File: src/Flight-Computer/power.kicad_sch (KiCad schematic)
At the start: 32 parts

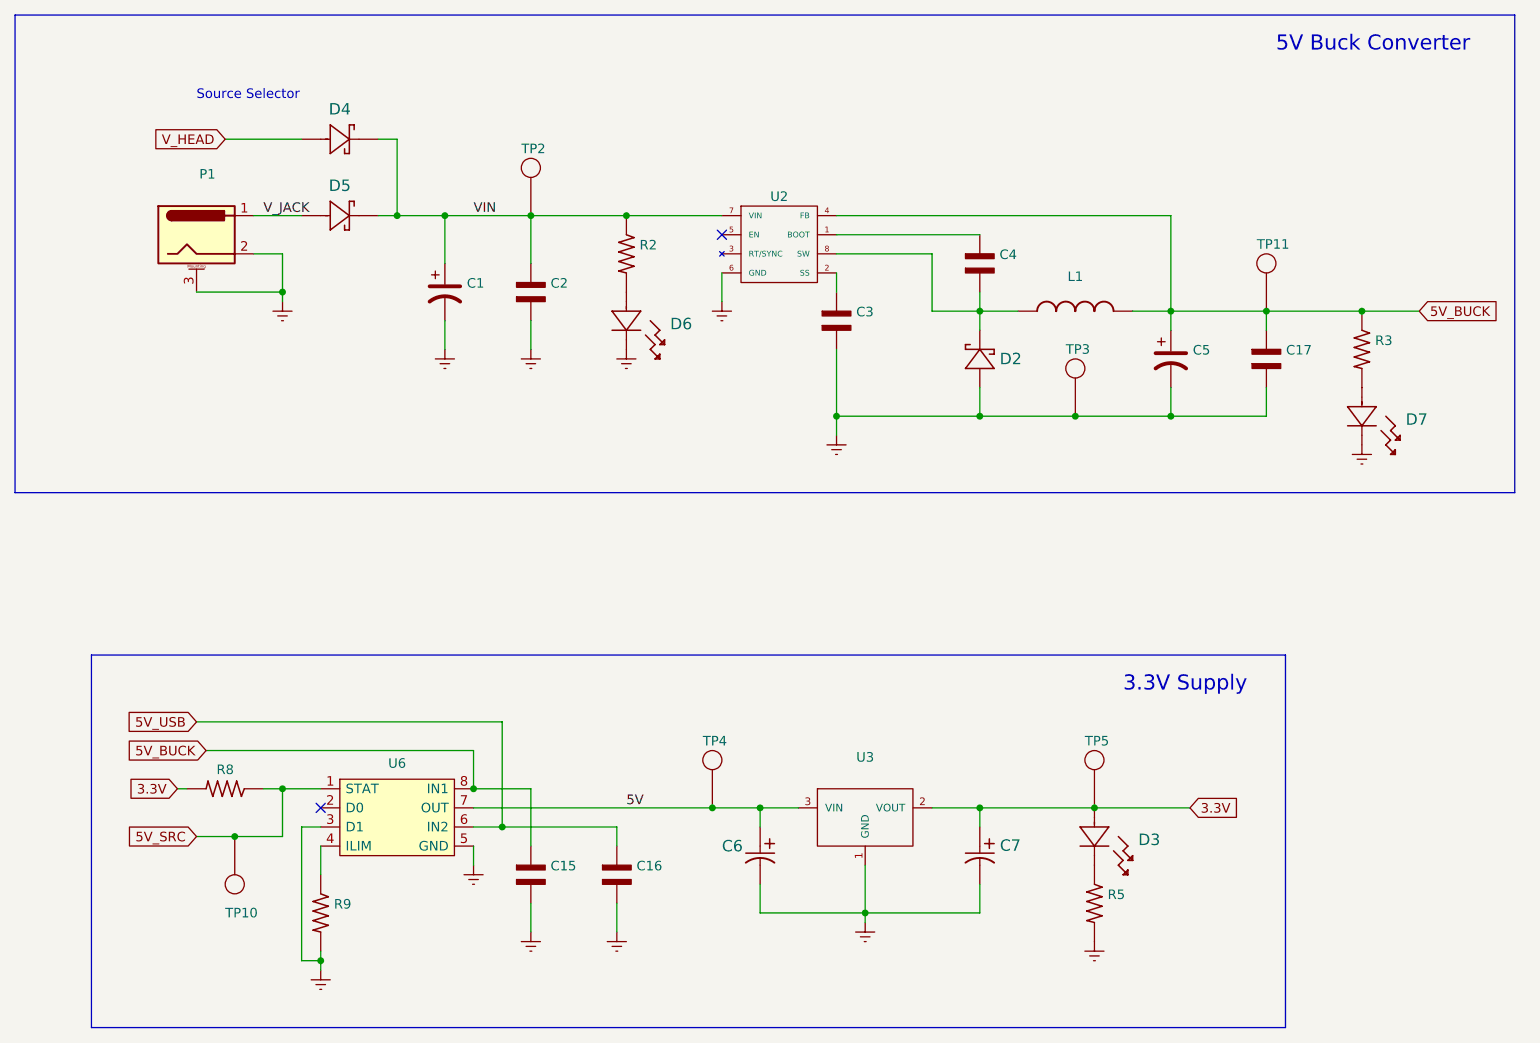
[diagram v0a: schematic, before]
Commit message: implemented crystal oscillator in schematic
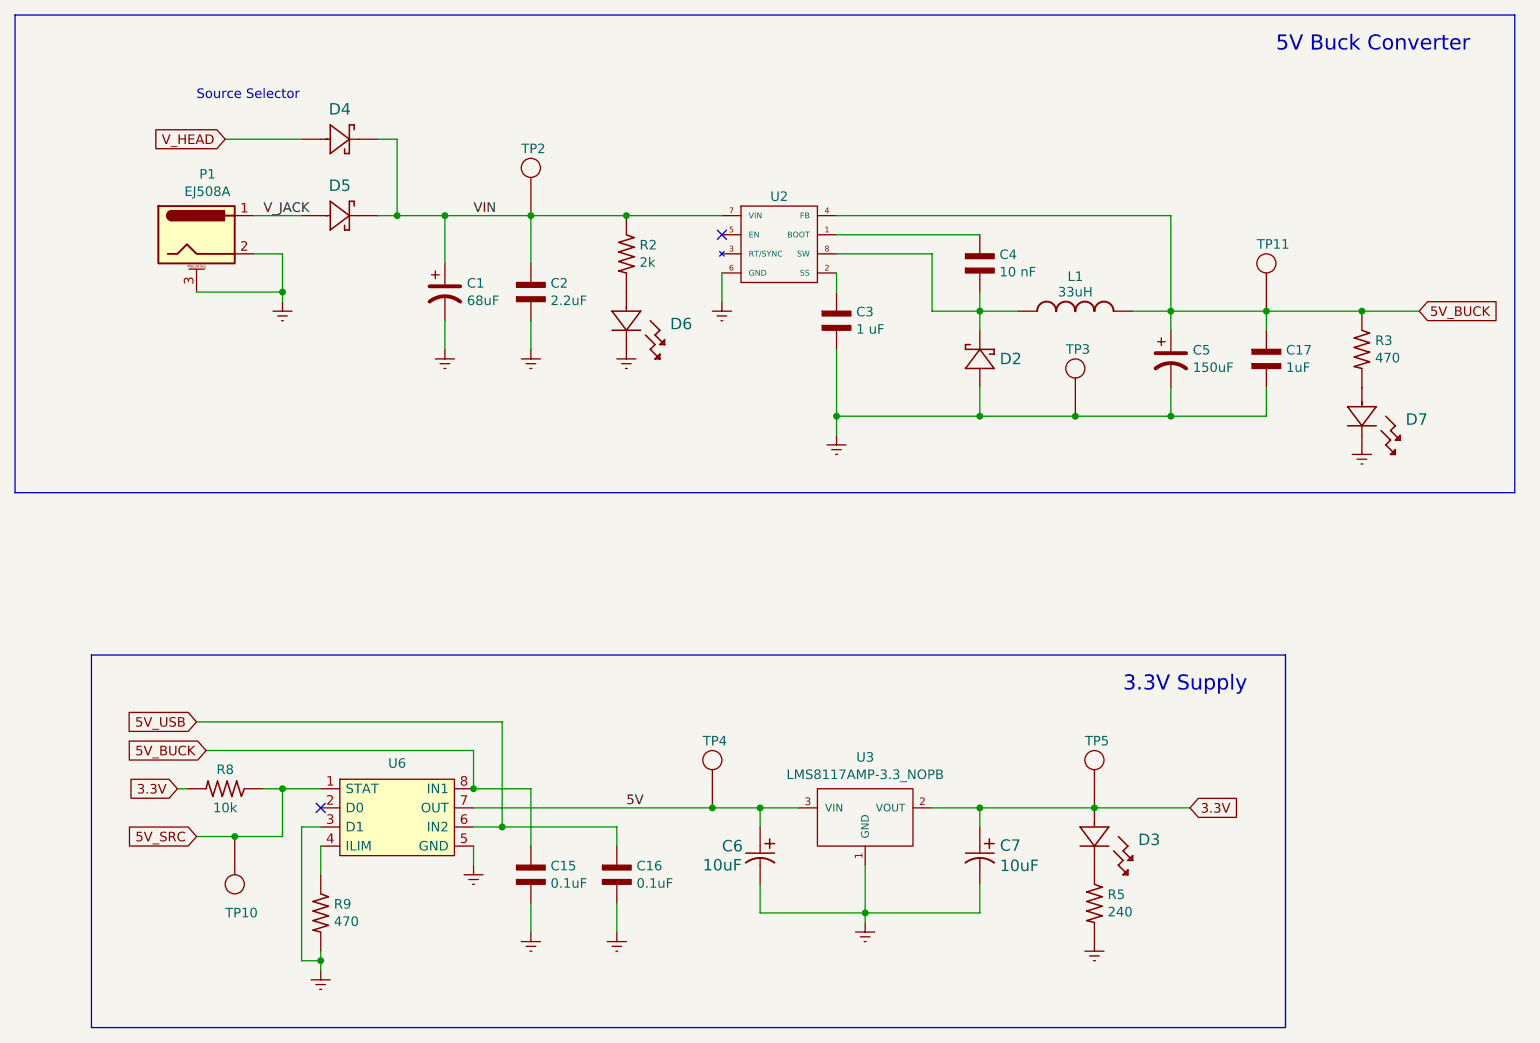
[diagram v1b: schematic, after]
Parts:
- C1: value (none) -> 68uF; footprint (none) -> Engine-Controller:EEEFPV680XAP
- C15, C16: value (none) -> 0.1uF; footprint (none) -> Engine-Controller:CAP_0603
- C17: value (none) -> 1uF; footprint (none) -> Engine-Controller:CAP_0603
- C2: value (none) -> 2.2uF; footprint (none) -> Engine-Controller:CAP_0603
- C3: value (none) -> 1 uF; footprint (none) -> Engine-Controller:CAP_0603
- C4: value (none) -> 10 nF; footprint (none) -> Engine-Controller:CAP_0603
- C5: value (none) -> 150uF; footprint (none) -> Engine-Controller:CAP_EEEFP1E151AL
- C6, C7: value (none) -> 10uF; footprint (none) -> Engine-Controller:CWR11HH106KB
- D2: value (none) -> RB160VAM-60TR; footprint (none) -> Engine-Controller:RB160VAM-60TR
- D3, D6, D7: value (none) -> SML-LX1206GC-TR; footprint (none) -> Engine-Controller:SML-LX1206GC-TR
- D4, D5: value (none) -> SM5819PL-TP; footprint (none) -> Engine-Controller:SM5819PL-TP
- L1: value (none) -> 33uH; footprint (none) -> Engine-Controller:SRP1038A-330M
- P1: value (none) -> EJ508A; footprint (none) -> Engine-Controller:12V_power_jack
- R2: value (none) -> 2k; footprint (none) -> Engine-Controller:RES_0603
- R3, R9: value (none) -> 470; footprint (none) -> Engine-Controller:RES_0603
- R5: value (none) -> 240; footprint (none) -> Engine-Controller:RES_0603
- R8: value (none) -> 10k; footprint (none) -> Engine-Controller:RES_0603
- TP10, TP11: value (none) -> TP; footprint (none) -> Engine-Controller:TP
- TP2: value (none) -> TPVIN; footprint (none) -> Engine-Controller:TP
- TP3: value (none) -> TPGND; footprint (none) -> Engine-Controller:TP
- TP4: value (none) -> TP5V; footprint (none) -> Engine-Controller:TP
- TP5: value (none) -> 3.3V; footprint (none) -> Engine-Controller:TP
- U2: value (none) -> LM22672MRE-5.0_NOPB; footprint (none) -> Engine-Controller:LM22672MRE-5.0_NOPB
- U3: value (none) -> LMS8117AMP-3.3_NOPB; footprint (none) -> Engine-Controller:SOT-223
- U6: value (none) -> TPS2115APWR; footprint (none) -> Engine-Controller:TPS2115APWR
